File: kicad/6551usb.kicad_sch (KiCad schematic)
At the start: 40 parts, among them J1 Conn_01x03_Male, P1 DLP-USB245R, SW1 SW_DIP_x06, U1 74LS04, U10 74LS74, U11 74LS86, U12 74LS33, U13 74LS273, U14 74LS374, U15 74LS244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

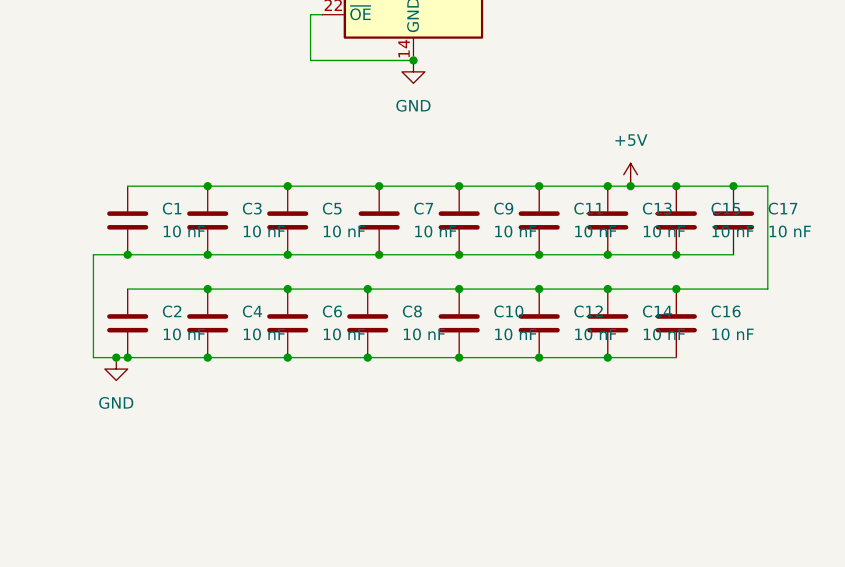
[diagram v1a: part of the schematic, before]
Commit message: v1.08: Updated to .1uf capacitors and slimmed width of card slightly
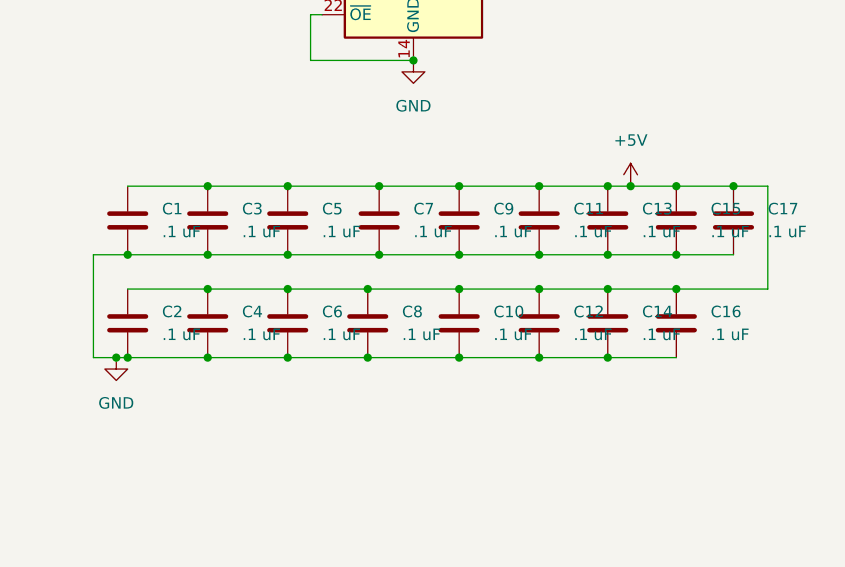
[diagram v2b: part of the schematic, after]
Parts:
- C1, C10, C11, C12, C13, C14, C15, C16, C17, C2, C3, C4, C5, C6, C7, C8, C9: value 10 nF -> .1 uF
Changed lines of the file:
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@@
   (title_block
     (title "CoCo USB Serial")
-    (date "2022-12-24")
-    (rev "1.07")
+    (date "2022-12-31")
+    (rev "1.08")
   )
   (junction (at 31.75 66.04) (diameter 0) (color 0 0 0 0)
@@
       (effects (font (size 1.27 1.27)) (justify left))
     )
-    (property "Value" "10 nF" (id 1) (at 416.56 214.6299 0)
+    (property "Value" ".1 uF" (id 1) (at 416.56 214.6299 0)
       (effects (font (size 1.27 1.27)) (justify left))
     )
@@
       (effects (font (size 1.27 1.27)) (justify left))
     )
-    (property "Value" "10 nF" (id 1) (at 367.03 226.0599 0)
+    (property "Value" ".1 uF" (id 1) (at 367.03 226.0599 0)
       (effects (font (size 1.27 1.27)) (justify left))
     )
@@
       (effects (font (size 1.27 1.27)) (justify left))
     )
-    (property "Value" "10 nF" (id 1) (at 410.21 226.0599 0)
+    (property "Value" ".1 uF" (id 1) (at 410.21 226.0599 0)
       (effects (font (size 1.27 1.27)) (justify left))
     )
@@
       (effects (font (size 1.27 1.27)) (justify left))
     )
-    (property "Value" "10 nF" (id 1) (at 394.97 226.0599 0)
+    (property "Value" ".1 uF" (id 1) (at 394.97 226.0599 0)
       (effects (font (size 1.27 1.27)) (justify left))
     )
@@
       (effects (font (size 1.27 1.27)) (justify left))
     )
-    (property "Value" "10 nF" (id 1) (at 402.59 214.6299 0)
+    (property "Value" ".1 uF" (id 1) (at 402.59 214.6299 0)
       (effects (font (size 1.27 1.27)) (justify left))
     )
@@
       (effects (font (size 1.27 1.27)) (justify left))
     )
-    (property "Value" "10 nF" (id 1) (at 358.14 214.6299 0)
+    (property "Value" ".1 uF" (id 1) (at 358.14 214.6299 0)
       (effects (font (size 1.27 1.27)) (justify left))
     )
@@
       (effects (font (size 1.27 1.27)) (justify left))
     )
-    (property "Value" "10 nF" (id 1) (at 386.08 226.0599 0)
+    (property "Value" ".1 uF" (id 1) (at 386.08 226.0599 0)
       (effects (font (size 1.27 1.27)) (justify left))
     )
@@
       (effects (font (size 1.27 1.27)) (justify left))
     )
-    (property "Value" "10 nF" (id 1) (at 358.14 226.0599 0)
+    (property "Value" ".1 uF" (id 1) (at 358.14 226.0599 0)
       (effects (font (size 1.27 1.27)) (justify left))
     )
@@
       (effects (font (size 1.27 1.27)) (justify left))
     )
-    (property "Value" "10 nF" (id 1) (at 349.25 226.0599 0)
+    (property "Value" ".1 uF" (id 1) (at 349.25 226.0599 0)
       (effects (font (size 1.27 1.27)) (justify left))
     )
@@
       (effects (font (size 1.27 1.27)) (justify left))
     )
-    (property "Value" "10 nF" (id 1) (at 394.97 214.6299 0)
+    (property "Value" ".1 uF" (id 1) (at 394.97 214.6299 0)
       (effects (font (size 1.27 1.27)) (justify left))
     )
@@
       (effects (font (size 1.27 1.27)) (justify left))
     )
-    (property "Value" "10 nF" (id 1) (at 386.08 214.6299 0)
+    (property "Value" ".1 uF" (id 1) (at 386.08 214.6299 0)
       (effects (font (size 1.27 1.27)) (justify left))
     )
@@
       (effects (font (size 1.27 1.27)) (justify left))
     )
-    (property "Value" "10 nF" (id 1) (at 349.25 214.6299 0)
+    (property "Value" ".1 uF" (id 1) (at 349.25 214.6299 0)
       (effects (font (size 1.27 1.27)) (justify left))
     )
@@
       (effects (font (size 1.27 1.27)) (justify left))
     )
-    (property "Value" "10 nF" (id 1) (at 377.19 214.6299 0)
+    (property "Value" ".1 uF" (id 1) (at 377.19 214.6299 0)
       (effects (font (size 1.27 1.27)) (justify left))
     )
@@
       (effects (font (size 1.27 1.27)) (justify left))
     )
-    (property "Value" "10 nF" (id 1) (at 402.59 226.0599 0)
+    (property "Value" ".1 uF" (id 1) (at 402.59 226.0599 0)
       (effects (font (size 1.27 1.27)) (justify left))
     )
@@
       (effects (font (size 1.27 1.27)) (justify left))
     )
-    (property "Value" "10 nF" (id 1) (at 375.92 226.0599 0)
+    (property "Value" ".1 uF" (id 1) (at 375.92 226.0599 0)
       (effects (font (size 1.27 1.27)) (justify left))
     )
@@
       (effects (font (size 1.27 1.27)) (justify left))
     )
-    (property "Value" "10 nF" (id 1) (at 367.03 214.6299 0)
+    (property "Value" ".1 uF" (id 1) (at 367.03 214.6299 0)
       (effects (font (size 1.27 1.27)) (justify left))
     )
@@
       (effects (font (size 1.27 1.27)) (justify left))
     )
-    (property "Value" "10 nF" (id 1) (at 410.21 214.6299 0)
+    (property "Value" ".1 uF" (id 1) (at 410.21 214.6299 0)
       (effects (font (size 1.27 1.27)) (justify left))
     )
@@
     )
     (path "/92900cd0-548c-482b-a1b2-9ce27355b8a5"
-      (reference "C1") (unit 1) (value "10 nF") (footprint "Capacitor_THT:C_Axial_L3.8mm_D2.6mm_P7.50mm_Horizontal")
+      (reference "C1") (unit 1) (value ".1 uF") (footprint "Capacitor_THT:C_Axial_L3.8mm_D2.6mm_P7.50mm_Horizontal")
     )
     (path "/5d109aee-10af-48e1-b2a9-3d1e1a8ec738"
-      (reference "C2") (unit 1) (value "10 nF") (footprint "Capacitor_THT:C_Axial_L3.8mm_D2.6mm_P7.50mm_Horizontal")
+      (reference "C2") (unit 1) (value ".1 uF") (footprint "Capacitor_THT:C_Axial_L3.8mm_D2.6mm_P7.50mm_Horizontal")
     )
     (path "/4166e586-3eef-490b-a5f6-91d900fba7db"
-      (reference "C3") (unit 1) (value "10 nF") (footprint "Capacitor_THT:C_Axial_L3.8mm_D2.6mm_P7.50mm_Horizontal")
+      (reference "C3") (unit 1) (value ".1 uF") (footprint "Capacitor_THT:C_Axial_L3.8mm_D2.6mm_P7.50mm_Horizontal")
     )
     (path "/4dd45b57-2389-4b20-93a0-c93afef743ec"
-      (reference "C4") (unit 1) (value "10 nF") (footprint "Capacitor_THT:C_Axial_L3.8mm_D2.6mm_P7.50mm_Horizontal")
+      (reference "C4") (unit 1) (value ".1 uF") (footprint "Capacitor_THT:C_Axial_L3.8mm_D2.6mm_P7.50mm_Horizontal")
     )
     (path "/e9df2569-c092-4dca-a2ce-78e0508d7836"
-      (reference "C5") (unit 1) (value "10 nF") (footprint "Capacitor_THT:C_Axial_L3.8mm_D2.6mm_P7.50mm_Horizontal")
+      (reference "C5") (unit 1) (value ".1 uF") (footprint "Capacitor_THT:C_Axial_L3.8mm_D2.6mm_P7.50mm_Horizontal")
     )
     (path "/19b98237-5f24-4c83-b332-8556720806a2"
-      (reference "C6") (unit 1) (value "10 nF") (footprint "Capacitor_THT:C_Axial_L3.8mm_D2.6mm_P7.50mm_Horizontal")
+      (reference "C6") (unit 1) (value ".1 uF") (footprint "Capacitor_THT:C_Axial_L3.8mm_D2.6mm_P7.50mm_Horizontal")
     )
     (path "/c81515ab-798c-4d77-9264-9747cfdc8a9b"
-      (reference "C7") (unit 1) (value "10 nF") (footprint "Capacitor_THT:C_Axial_L3.8mm_D2.6mm_P7.50mm_Horizontal")
+      (reference "C7") (unit 1) (value ".1 uF") (footprint "Capacitor_THT:C_Axial_L3.8mm_D2.6mm_P7.50mm_Horizontal")
     )
     (path "/e6da5f6f-c6f7-4b06-b3ad-c84e899a31d1"
-      (reference "C8") (unit 1) (value "10 nF") (footprint "Capacitor_THT:C_Axial_L3.8mm_D2.6mm_P7.50mm_Horizontal")
+      (reference "C8") (unit 1) (value ".1 uF") (footprint "Capacitor_THT:C_Axial_L3.8mm_D2.6mm_P7.50mm_Horizontal")
     )
     (path "/8ab98215-c1fc-48c8-a81c-a796ad530446"
-      (reference "C9") (unit 1) (value "10 nF") (footprint "Capacitor_THT:C_Axial_L3.8mm_D2.6mm_P7.50mm_Horizontal")
+      (reference "C9") (unit 1) (value ".1 uF") (footprint "Capacitor_THT:C_Axial_L3.8mm_D2.6mm_P7.50mm_Horizontal")
     )
     (path "/4c1467d0-d50f-4552-a20a-6e2efa1c74aa"
-      (reference "C10") (unit 1) (value "10 nF") (footprint "Capacitor_THT:C_Axial_L3.8mm_D2.6mm_P7.50mm_Horizontal")
+      (reference "C10") (unit 1) (value ".1 uF") (footprint "Capacitor_THT:C_Axial_L3.8mm_D2.6mm_P7.50mm_Horizontal")
     )
     (path "/761b09f2-6065-44da-acb0-1824fa7d920b"
-      (reference "C11") (unit 1) (value "10 nF") (footprint "Capacitor_THT:C_Axial_L3.8mm_D2.6mm_P7.50mm_Horizontal")
+      (reference "C11") (unit 1) (value ".1 uF") (footprint "Capacitor_THT:C_Axial_L3.8mm_D2.6mm_P7.50mm_Horizontal")
     )
     (path "/3410e812-d04b-4aed-adc2-fa2c7dc620eb"
-      (reference "C12") (unit 1) (value "10 nF") (footprint "Capacitor_THT:C_Axial_L3.8mm_D2.6mm_P7.50mm_Horizontal")
+      (reference "C12") (unit 1) (value ".1 uF") (footprint "Capacitor_THT:C_Axial_L3.8mm_D2.6mm_P7.50mm_Horizontal")
     )
     (path "/3ad80298-ceea-4736-b529-e5291a0387f8"
-      (reference "C13") (unit 1) (value "10 nF") (footprint "Capacitor_THT:C_Axial_L3.8mm_D2.6mm_P7.50mm_Horizontal")
+      (reference "C13") (unit 1) (value ".1 uF") (footprint "Capacitor_THT:C_Axial_L3.8mm_D2.6mm_P7.50mm_Horizontal")
     )
     (path "/cf4721bd-bf69-4219-a198-cb20285b27a8"
-      (reference "C14") (unit 1) (value "10 nF") (footprint "Capacitor_THT:C_Axial_L3.8mm_D2.6mm_P7.50mm_Horizontal")
+      (reference "C14") (unit 1) (value ".1 uF") (footprint "Capacitor_THT:C_Axial_L3.8mm_D2.6mm_P7.50mm_Horizontal")
     )
     (path "/efccf67c-b529-4dd1-bdc1-59fad0fa3efb"
-      (reference "C15") (unit 1) (value "10 nF") (footprint "Capacitor_THT:C_Axial_L3.8mm_D2.6mm_P7.50mm_Horizontal")
+      (reference "C15") (unit 1) (value ".1 uF") (footprint "Capacitor_THT:C_Axial_L3.8mm_D2.6mm_P7.50mm_Horizontal")
     )
     (path "/313cd128-e1ae-4ae0-9717-1fd7d24a5138"
-      (reference "C16") (unit 1) (value "10 nF") (footprint "Capacitor_THT:C_Axial_L3.8mm_D2.6mm_P7.50mm_Horizontal")
+      (reference "C16") (unit 1) (value ".1 uF") (footprint "Capacitor_THT:C_Axial_L3.8mm_D2.6mm_P7.50mm_Horizontal")
     )
     (path "/13cd2c16-b1e1-4f5a-a9f0-98230ed457a5"
-      (reference "C17") (unit 1) (value "10 nF") (footprint "Capacitor_THT:C_Axial_L3.8mm_D2.6mm_P7.50mm_Horizontal")
+      (reference "C17") (unit 1) (value ".1 uF") (footprint "Capacitor_THT:C_Axial_L3.8mm_D2.6mm_P7.50mm_Horizontal")
     )
     (path "/f11e73d1-550d-4cc2-a4f9-509efb462117"

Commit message: Updated to version 1.09 with usb module power jumper
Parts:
- added JP1: Jumper_3_Open, Connector_PinHeader_2.54mm:PinHeader_1x03_P2.54mm_Vertical, symbol Jumper:Jumper_3_Open
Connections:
- net +5V: now also JP1.3 (B); no longer P1.7 (VCCIO)
- net at P1.9 (PORTVCC): now also JP1.1 (A)
- new net: JP1.2 (C), P1.7 (VCCIO)
- no-connect marks 22 -> 21
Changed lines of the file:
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@@
   (title_block
     (title "CoCo USB Serial")
-    (date "2022-12-31")
-    (rev "1.08")
+    (date "2023-05-14")
+    (rev "1.09")
   )
   (junction (at 31.75 66.04) (diameter 0) (color 0 0 0 0)
@@
   (junction (at 354.33 217.17) (diameter 0) (color 0 0 0 0)
   )
-  (junction (at 297.18 80.01) (diameter 0) (color 0 0 0 0)
-  )
   (junction (at 354.33 228.6) (diameter 0) (color 0 0 0 0)
   )
@@
   (junction (at 39.37 210.82) (diameter 0) (color 0 0 0 0)
   )
+  (junction (at 298.45 80.01) (diameter 0) (color 0 0 0 0)
+  )
   (junction (at 372.11 228.6) (diameter 0) (color 0 0 0 0)
   )
@@
   (junction (at 354.33 209.55) (diameter 0) (color 0 0 0 0)
   )
+  (junction (at 300.99 80.01) (diameter 0) (color 0 0 0 0)
+  )
   (junction (at 388.62 100.33) (diameter 0) (color 0 0 0 0)
   )
@@
   (junction (at 220.98 227.33) (diameter 0) (color 0 0 0 0)
   )
-  (junction (at 297.18 82.55) (diameter 0) (color 0 0 0 0)
-  )
   (junction (at 375.92 96.52) (diameter 0) (color 0 0 0 0)
   )
@@
   (no_connect (at 39.37 203.2))
   (no_connect (at 414.02 38.1))
-  (no_connect (at 285.75 80.01))
   (no_connect (at 383.54 53.34))
   (no_connect (at 383.54 38.1))
@@
     (stroke (width 0) (type default) (color 0 0 0 0))
   )
-  (wire (pts (xy 285.75 85.09) (xy 297.18 85.09))
-    (stroke (width 0) (type default) (color 0 0 0 0))
-  )
   (wire (pts (xy 135.89 205.74) (xy 135.89 207.01))
     (stroke (width 0) (type default) (color 0 0 0 0))
@@
     (stroke (width 0) (type default) (color 0 0 0 0))
   )
-  (wire (pts (xy 297.18 80.01) (xy 300.99 80.01))
-    (stroke (width 0) (type default) (color 0 0 0 0))
-  )
   (wire (pts (xy 87.63 86.36) (xy 87.63 102.87))
     (stroke (width 0) (type default) (color 0 0 0 0))
@@
     (stroke (width 0) (type default) (color 0 0 0 0))
   )
+  (wire (pts (xy 298.45 67.31) (xy 298.45 80.01))
+    (stroke (width 0) (type default) (color 0 0 0 0))
+  )
   (wire (pts (xy 200.66 60.96) (xy 209.55 60.96))
     (stroke (width 0) (type default) (color 0 0 0 0))
@@
     (stroke (width 0) (type default) (color 0 0 0 0))
   )
+  (wire (pts (xy 285.75 67.31) (xy 285.75 80.01))
+    (stroke (width 0) (type default) (color 0 0 0 0))
+  )
   (bus (pts (xy 259.08 133.35) (xy 259.08 135.89))
     (stroke (width 0) (type default) (color 0 0 0 0))
@@
     (stroke (width 0) (type default) (color 0 0 0 0))
   )
-  (wire (pts (xy 285.75 82.55) (xy 297.18 82.55))
+  (wire (pts (xy 285.75 82.55) (xy 298.45 82.55))
     (stroke (width 0) (type default) (color 0 0 0 0))
   )
@@
     (stroke (width 0) (type default) (color 0 0 0 0))
   )
-  (wire (pts (xy 297.18 82.55) (xy 297.18 80.01))
+  (wire (pts (xy 298.45 82.55) (xy 298.45 80.01))
     (stroke (width 0) (type default) (color 0 0 0 0))
   )
@@
     (stroke (width 0) (type default) (color 0 0 0 0))
   )
-  (wire (pts (xy 297.18 80.01) (xy 297.18 78.74))
-    (stroke (width 0) (type default) (color 0 0 0 0))
-  )
   (wire (pts (xy 322.58 140.97) (xy 323.85 140.97))
     (stroke (width 0) (type default) (color 0 0 0 0))
@@
     (stroke (width 0) (type default) (color 0 0 0 0))
   )
+  (wire (pts (xy 298.45 80.01) (xy 300.99 80.01))
+    (stroke (width 0) (type default) (color 0 0 0 0))
+  )
   (wire (pts (xy 215.9 196.85) (xy 219.71 196.85))
     (stroke (width 0) (type default) (color 0 0 0 0))
@@
     (stroke (width 0) (type default) (color 0 0 0 0))
   )
+  (wire (pts (xy 292.1 71.12) (xy 292.1 85.09))
+    (stroke (width 0) (type default) (color 0 0 0 0))
+  )
   (wire (pts (xy 204.47 148.59) (xy 204.47 165.1))
     (stroke (width 0) (type default) (color 0 0 0 0))
@@
     (stroke (width 0) (type default) (color 0 0 0 0))
   )
-  (wire (pts (xy 297.18 82.55) (xy 297.18 85.09))
-    (stroke (width 0) (type default) (color 0 0 0 0))
-  )
   (wire (pts (xy 36.83 151.13) (xy 36.83 153.67))
     (stroke (width 0) (type default) (color 0 0 0 0))
@@
     (stroke (width 0) (type default) (color 0 0 0 0))
   )
+  (wire (pts (xy 285.75 85.09) (xy 292.1 85.09))
+    (stroke (width 0) (type default) (color 0 0 0 0))
+  )
   (wire (pts (xy 398.78 228.6) (xy 406.4 228.6))
     (stroke (width 0) (type default) (color 0 0 0 0))
@@
     (pin "7")
   )
+  (symbol (lib_id "Jumper:Jumper_3_Open") (at 292.1 67.31 0) (unit 1)
+    (in_bom yes) (on_board yes) (fields_autoplaced)
+    (property "Reference" "JP1" (id 0) (at 292.1 60.96 0))
+    (property "Value" "Jumper_3_Open" (id 1) (at 292.1 63.5 0))
+    (property "Footprint" "Connector_PinHeader_2.54mm:PinHeader_1x03_P2.54mm_Vertical" (id 2) (at 292.1 67.31 0)
+      (effects (font (size 1.27 1.27)) hide)
+    )
+    (property "Datasheet" "~" (id 3) (at 292.1 67.31 0)
+      (effects (font (size 1.27 1.27)) hide)
+    )
+    (pin "1")
+    (pin "2")
+    (pin "3")
+  )
   (symbol (lib_id "74xx:74LS00") (at 215.9 45.72 0) (unit 1)
     (in_bom yes) (on_board yes) (fields_autoplaced)
@@
     (pin "7")
   )
-  (symbol (lib_id "power:+5V") (at 297.18 78.74 0) (unit 1)
+  (symbol (lib_id "power:+5V") (at 300.99 80.01 0) (unit 1)
     (in_bom yes) (on_board yes)
-    (property "Reference" "#PWR0110" (id 0) (at 297.18 82.55 0)
+    (property "Reference" "#PWR0110" (id 0) (at 300.99 83.82 0)
       (effects (font (size 1.27 1.27)) hide)
     )
-    (property "Value" "+5V" (id 1) (at 297.18 73.66 0))
-    (property "Footprint" "" (id 2) (at 297.18 78.74 0)
+    (property "Value" "+5V" (id 1) (at 300.99 74.93 0))
+    (property "Footprint" "" (id 2) (at 300.99 80.01 0)
       (effects (font (size 1.27 1.27)) hide)
     )
-    (property "Datasheet" "" (id 3) (at 297.18 78.74 0)
+    (property "Datasheet" "" (id 3) (at 300.99 80.01 0)
       (effects (font (size 1.27 1.27)) hide)
     )
@@
       (reference "J1") (unit 1) (value "Conn_01x03_Male") (footprint "Connector_PinHeader_2.54mm:PinHeader_1x03_P2.54mm_Vertical")
     )
+    (path "/8029017d-056a-400b-81cc-fd0942e56f27"
+      (reference "JP1") (unit 1) (value "Jumper_3_Open") (footprint "Connector_PinHeader_2.54mm:PinHeader_1x03_P2.54mm_Vertical")
+    )
     (path "/e683bc92-d8a0-46fd-94c4-362ea9e7214a"
